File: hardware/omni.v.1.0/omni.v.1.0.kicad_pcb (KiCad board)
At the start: 4 copper layers, 33.7 x 19 mm, 81 parts, among them J101 USB_B_Micro, U101 MDBT50Q-1MV2, U102 MCP1703A-4002_SOT23

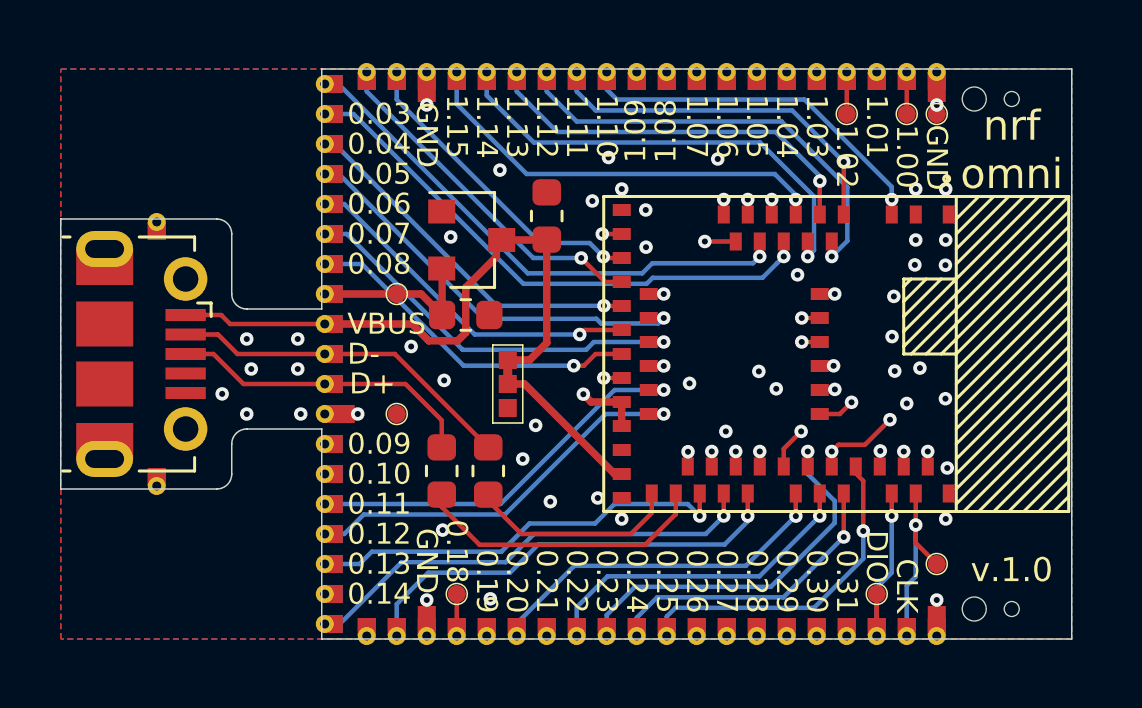
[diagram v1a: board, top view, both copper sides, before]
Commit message: moved castellated holes closer to edge cut
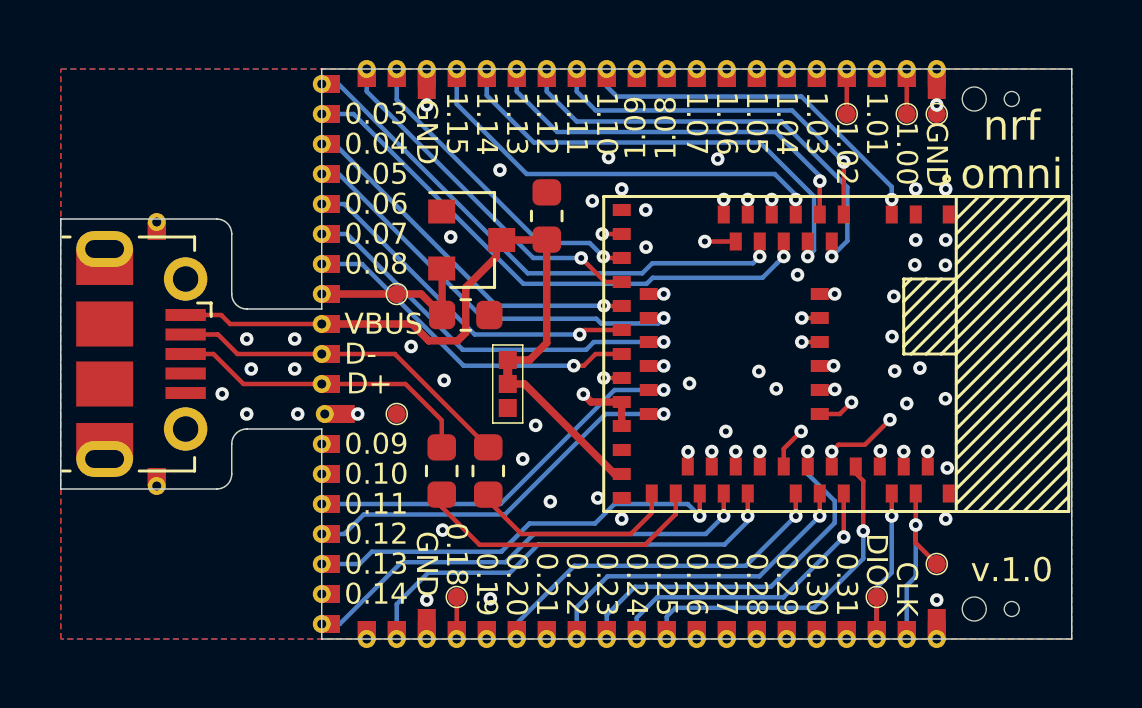
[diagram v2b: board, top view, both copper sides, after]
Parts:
- moved TP101 0.10 mm to (109.5, 97.5)
- moved TP102 0.10 mm to (108.5, 97.5)
- moved TP103 0.10 mm to (107.5, 97.5)
- moved TP104 0.10 mm to (106.5, 97.5)
- moved TP105 0.10 mm to (105.5, 97.5)
- moved TP106 0.10 mm to (104.5, 97.5)
- moved TP107 0.10 mm to (100.0, 99.0)
- moved TP108 0.10 mm to (115.5, 116.5)
- moved TP109 0.10 mm to (100.0, 98.0)
- moved TP110 0.10 mm to (117.5, 116.5)
- moved TP111 0.10 mm to (114.5, 116.5)
- moved TP112 0.10 mm to (116.5, 116.5)
- moved TP113 0.10 mm to (113.5, 116.5)
- moved TP114 0.10 mm to (102.5, 97.5)
- moved TP115 0.10 mm to (101.5, 97.5)
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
